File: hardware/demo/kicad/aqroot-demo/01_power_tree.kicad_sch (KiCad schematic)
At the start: 138 parts, among them J3 USB_C_Receptacle_USB2.0_16P, J4 BATTERY PIGTAIL 26AWG, Q2 NTMD4820N, Q3 NTMD4820N, Q4 BSS138, Q5 AO3401A, Q6 BSS138, Q7 BSS138, Q8 BSS138, Q9 BSS138, SW9 SW_SPDT, U10 USBLC6-2SC6, U11 BQ25185, U12 TPS63020, U13 TPS61023, U14 MAX17048, U18 LTC4368-1, U19 TLV7032, U20 TPS22950-Q1, U21 TPS61023, U22 TPS22950-Q1

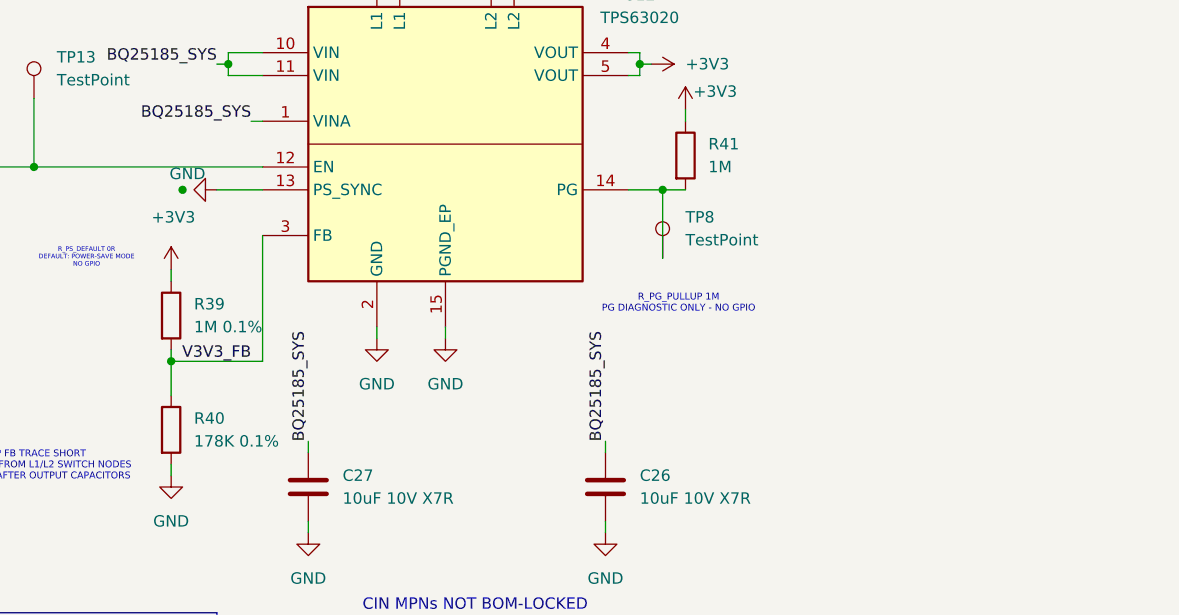
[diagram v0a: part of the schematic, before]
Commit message: demo: D-788 close Round-7 and centre the +3V3 rail inside the display's absolute maximum
Round-7 external review REJECTED D-787.  Astra reproduced 20 observed release
defects (6 high, 6 medium, 8 low) and Fable reproduced a subset plus a sourcing
concern.  All twenty are closed.  Auditing the candidate against its own primary
sources found SIX MORE, R7-N01..R7-N06, and the first two moved the board.

THE HIGH ONE.  The fitted ER-TFT035IPS-6 is an ILI9488 panel whose own datasheet
(archived vendor/ILITEK/ilitek-ili9488-v100.pdf, Table 41) makes 3.3 V the
ABSOLUTE MAXIMUM on both VCI and IOVCC.  D-787's power-save corner stood 242 mV
over it and its NOMINAL stood 9 mV over it.  Closed with two objects and no new
component: U12's PS/SYNC moves GND -> EN (forced fixed-frequency PWM, so TI's
VFB_PS +5 % excursion cannot occur) and the feedback divider moves down.

R7-N01/R7-N02, FOUND HERE.  A DC bound is not the whole high side -- ripple and
load-transient overshoot ride on top of it -- and the low side had NO MCU clause
at all: the rail minimum was checked against the panel's VCI 2.5 V and the
Community Port's published minimum, never against the ESP32-S3-WROOM-1's own
3.0 V VDD33 row.  The first D-788 draft's 187 kOhm left 47.97 mV under a DAMAGE
limit against 86.36 mV over a RECOVERABLE one, which is the wrong way round.
F6 now computes the ripple (1.68 mV pp from SLVS916I's minimum oscillator
frequency and L1's minimum inductance), charges it to both ends, adds the module
floor and the +3V3 plane's bounded distribution drop, and ENUMERATES every
purchasable E192 0.1 % R40 value -- requiring the fitted one to maximise the
smaller of the two headrooms.  R40 is therefore 189 kOhm (YAGEO
RT0603BRD07189KL, C861174, live stock 339), splitting it 76.99 / 58.78 mV.
Load-transient overshoot is deliberately given NO analytic bound, because TI
publishes it only as 50 mV/div plots; it is measured at first article as the new
C-PWR-TRANSIENT-01, and the lever if it fails is C29-C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
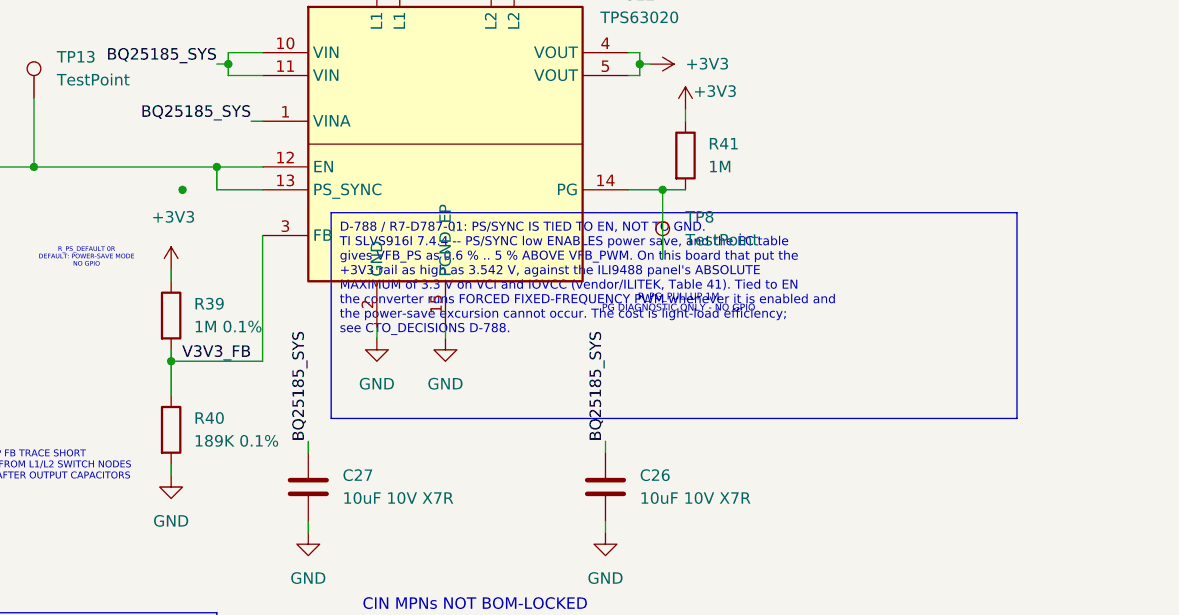
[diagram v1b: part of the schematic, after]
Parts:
- R40: value 178K 0.1% -> 189K 0.1%; LCSC C2441185 -> C861174; MPN ARG03BTC1783 -> RT0603BRD07189KL; Manufacturer Viking Tech -> YAGEO; Note D-787 / R6-A01 THE MAIN 3.3 V RAIL IS ADJUSTABLE AND ITS SE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 -> D-788 / R7-D787-01 + R7-N01. THE RAIL HAD NO CEILING AND TH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; Note_Sourcing SOURCING D-787 2026-09-20, verified live per D-096 through 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 -> SOURCING D-788 2026-09-20, verified live per D-096 through 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
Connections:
- net GND: no longer U12.13 (PS_SYNC)
- net at R43.1, R68.2, SW9.1 (A)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: now also U12.13 (PS_SYNC)
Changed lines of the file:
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@@
 			)
 		)
-		(property "Value" "178K 0.1%"
+		(property "Value" "189K 0.1%"
 			(at 220.98 100.3299 0)
 			(show_name no)
@@
 			)
 		)
-		(property "Manufacturer" "Viking Tech"
+		(property "Manufacturer" "YAGEO"
 			(at 218.44 99.06 0)
 			(hide yes)
@@
 			)
 		)
-		(property "MPN" "ARG03BTC1783"
+		(property "MPN" "RT0603BRD07189KL"
 			(at 218.44 99.06 0)
 			(hide yes)
@@
 			)
 		)
-		(property "LCSC" "C2441185"
+		(property "LCSC" "C861174"
 			(at 218.44 99.06 0)
 			(hide yes)
@@
 			)
 		)
-		(property "Note_Sourcing" "SOURCING D-787 2026-09-20, verified live per D-096 through the JLCPCB parts API.  LCSC C2441185, Viking Tech ARG03BTC1783, 178 kOhm +/-0.1 pct, 0603, 100 mW thin film, +/-25 ppm/C, -55..+155 C, componentLibraryType = expand, stock 3973 (evidence/jlc-live/arg03btc1783-*.json).  SAME Viking ARG03B SERIES AND SAME 0.1 pct / 25 ppm GRADE as R39, so the divider's two halves track.  This REPLACES the D-614 line 'EXACT_PRIOR from the beta-dm audit line 180K 1 pct', which sourced UNI-ROYAL 0603WAF1803T5E C22827.  176 kOhm WAS THE FIRST D-787 CANDIDATE AND IS REFUSED ON AVAILABILITY, not on electricals: every 176 kOhm 0603 part at 0.1 pct or better in the JLCPCB catalogue reads stock 0 -- including the KOA RN73H1JTTD1763B10 C4086101 that draft named (evidence/jlc-live/176k-0603-0-1-*.json) -- so it fails this project's own rule_open_sourcing stock floor of 5 boards x 10 liquidity.  178 kOhm is the nearest STOCKED 0.1 pct value that keeps the derived envelope inside BOTH the 3.135 V Community Port minimum and the 3.600 V internal consumer maximum, and it is also the low-side magnitude TI's own SLVS916I Table 3 prints for a 3.3 V output.  Same 0603 land: no footprint, no copper and no assembly step change."
+		(property "Note_Sourcing" "SOURCING D-788 2026-09-20, verified live per D-096 through the JLCPCB parts API.  LCSC C861174, YAGEO RT0603BRD07189KL, 189 kOhm +/-0.1 pct, 0603, thin film, +/-25 ppm/C, -55..+155 C, componentLibraryType = expand, stock 339 (evidence/jlc-live/rt0603brd07189kl-*.json and 189k-0-1-0603-*.json).  339 is 68x the five-board need of 5 and clears this repository's hard liquidity gate (5 parts x 5 boards x 10 = 50); it is BELOW the 500-piece comfort floor, so rule_open_sourcing carries it as a THIN line and the pre-PCBA stock re-check owns it.  SAME 0.1 pct / 25 ppm GRADE, same YAGEO RT0603 family and the same 0603 land as the 187 kOhm RT0603BRD07187KL C861172 it replaces, so the divider's two halves still track and F6's MPN-keyed temperature-coefficient table needs only the new row.  WAS 187 kOhm RT0603BRD07187KL C861172 (D-788 first draft); WAS 178 kOhm Viking ARG03BTC1783 C2441185 (D-787).  189 kOhm is the E192 value that CENTRES the rail's own tolerance band inside the 3.000..3.300 V window the ESP32-S3 floor and the ILI9488 absolute maximum leave; 191 kOhm overshoots (42.5 mV to the MCU floor) and 188 kOhm is not an E192 value."
 			(at 218.44 99.06 0)
 			(hide yes)
@@
 			)
 		)
-		(property "Note" "D-787 / R6-A01 THE MAIN 3.3 V RAIL IS ADJUSTABLE AND ITS SETPOINT WAS NEVER A PROOF TERM.  Every accessory clause before D-787 ran on a TYPED 3.3 V constant, so the released 1 MOhm / 180 kOhm 1 pct divider could sit anywhere in a band the contract could not see, and F6 stayed green while the Community Port's PUBLISHED 3.135 V minimum was not guaranteed at the PUBLISHED 400 mA.  F6 now DERIVES the whole envelope: TI SLVS916I VFB_PWM 495 / 500 / 505 mV, the fitted value tolerance, the SELECTED PART's temperature coefficient over -40..+85 C, TI's 0.5 pct maximum line and 0.5 pct maximum load regulation applied together, and the +5 pct power-save high side checked separately.  At R39 = 1 MOhm and R40 = 178 kOhm, both Viking ARG03B 0.1 pct / 25 ppm, the raw PWM band is 3.261337 / 3.308989 / 3.357013 V, the heavy-load minimum is 3.228806 V and the power-save high side is 3.542487 V against the 3.600 V tightest internal consumer maximum.  DELIVERY IS A SEPARATE CLAUSE: the bounded hot U20->TP12 prefix, the manual first-five reinforcement lead at its <=30 mOhm acceptance and U20's 68 mOhm maximum RON cost 82.4 mV at 400 mA, leaving 3.146366 V at either duplicated 3.3 V contact.  THE WINDOW IS NARROW IN BOTH DIRECTIONS -- 180 kOhm falls below the connector minimum and 174 kOhm exceeds the internal consumer maximum -- which is why the divider's tolerance grade and temperature coefficient are locked by F7 and why F6 refuses an MPN whose coefficient this repository has not read.  WAS 180 kOhm 1 pct (D-614).  Pinned by checks/demo_feature_contract.py F6 and F7."
+		(property "Note" "D-788 / R7-D787-01 + R7-N01.  THE RAIL HAD NO CEILING AND THE DISPLAY'S ABSOLUTE MAXIMUM IS 3.3 V.  D-787 judged the rail's high side against a 3.600 V 'tightest internal consumer' that was FALSE.  The fitted ER-TFT035IPS-6 is an ILI9488 panel, and ILI Technology's own datasheet -- archived at vendor/ILITEK/ilitek-ili9488-v100.pdf, sha256 aeb23170f809610458e05ab514a5e3017344938ccdba1c2031acb453941df38b, corroborated against a second independent mirror -- gives in Table 41 an ABSOLUTE MAXIMUM of -0.3 .. +3.3 V for BOTH VCI ~ DGND and IOVCC ~ DGND, and in section 17.2 a DC operating range of VCI 2.5 / 2.8 / 3.3 V and IOVCC 1.65 / 1.8 / 3.3 V with VIH max = IOVCC.  D-787's derived power-save high side was 3.542487 V -- 242 mV over an ABSOLUTE MAXIMUM -- and even its NOMINAL 3.308989 V stood 9 mV above it.  D-788 closes it with TWO changes and NO new component: U12's PS/SYNC moves from GND to the EN net so the converter runs FORCED FIXED-FREQUENCY PWM and TI's VFB_PS +5 pct power-save excursion cannot occur, and this divider moves the whole band down.  R7-N01 THEN CENTRES IT: a DC-only bound is not the whole high side, because ripple and load-transient overshoot ride on top of it and TI plots this converter's own load transient at 50 mV/div for a 1 A step (SLVS916I Figures 21/22).  187 kOhm left only 47.97 mV of DC headroom under a DAMAGE limit while leaving 96.99 mV over the ESP32-S3's RECOVERABLE 3.0 V floor; 189 kOhm splits that 76.98 / 69.41 mV, which is where the window centres once the +3V3 plane's own few millivolts of distribution drop are counted on the MCU side.  Raw PWM band 3.100334 / 3.145503 / 3.191022 V, heavy-load minimum 3.069405 V, worst case 3.223016 V.  Display VCI/IOVCC and the MCU remain the SAME net, so VIH <= IOVCC holds by construction and no display input is ever driven above its own supply.  THE COST IS THE COMMUNITY PORT: a rail whose maximum must stay under 3.3 V cannot also guarantee 3.3 V -5 pct at the connector at ANY current.  The owner approved OPTION A on 2026-09-20 and delegated the exact values to the final candidate; this one delivers 2.954958 V at the published 400 mA.  Pinned by checks/demo_feature_contract.py F6 and F7."
 			(at 218.44 99.06 0)
 			(hide yes)
@@
 	(symbol
 		(lib_id "power:GND")
-		(at 223.52 72.39 270)
-		(unit 1)
-		(body_style 1)
-		(exclude_from_sim no)
-		(in_bom yes)
-		(on_board yes)
-		(in_pos_files yes)
-		(dnp no)
-		(property "Reference" "#PWR0146"
-			(at 217.17 72.39 0)
-			(hide yes)
-			(show_name no)
-			(do_not_autoplace no)
-			(effects
-				(font
-					(size 1.27 1.27)
-				)
-			)
-		)
-		(property "Value" "GND"
-			(at 222.25 70.612 90)
-			(show_name no)
-			(do_not_autoplace no)
-			(effects
-				(font
-					(size 1.27 1.27)
-				)
-				(justify right)
-			)
-		)
-		(property "Footprint" ""
-			(at 223.52 72.39 0)
-			(hide yes)
-			(show_name no)
-			(do_not_autoplace no)
-			(effects
-				(font
-					(size 1.27 1.27)
-				)
-			)
-		)
-		(property "Datasheet" ""
-			(at 223.52 72.39 0)
-			(hide yes)
-			(show_name no)
-			(do_not_autoplace no)
-			(effects
-				(font
-					(size 1.27 1.27)
-				)
-			)
-		)
-		(property "Description" "Power symbol creates a global label with name \"GND\" , ground"
-			(at 223.52 72.39 0)
-			(hide yes)
-			(show_name no)
-			(do_not_autoplace no)
-			(effects
-				(font
-					(size 1.27 1.27)
-				)
-			)
-		)
-		(pin "1"
-		)
-		(instances
-			(project "aqroot-Beta-v2"
-				(path "/8a0ad1ee-a49e-4cff-9a78-44823e373405/83b1880a-0a3b-496a-bce6-0dc4c72d8ece"
-					(reference "#PWR0146")
-					(unit 1)
-				)
-			)
-		)
-	)
-	(symbol
-		(lib_id "power:GND")
 		(at 29.21 171.45 0)
 		(unit 1)
@@
 		)
 	)
+	(wire
+		(pts
+			(xy 223.52 72.39) (xy 223.52 69.85)
+		)
+		(stroke
+			(width 0)
+			(type default)
+		)
+	)
+	(junction
+		(at 223.52 69.85)
+		(diameter 0)
+		(color 0 0 0 0)
+	)
+	(text_box "D-788 / R7-D787-01: PS/SYNC IS TIED TO EN, NOT TO GND.\nTI SLVS916I 7.4.4 -- PS/SYNC low ENABLES power save, and the EC table\n gives VFB_PS as 0.6 % .. 5 % ABOVE VFB_PWM. On this board that put the\n+3V3 rail as high as 3.542 V, against the ILI9488 panel's ABSOLUTE\nMAXIMUM of 3.3 V on VCI and IOVCC (vendor/ILITEK, Table 41). Tied to EN\nthe converter runs FORCED FIXED-FREQUENCY PWM whenever it is enabled and\nthe power-save excursion cannot occur. The cost is light-load efficiency;\nsee CTO_DECISIONS D-788."
+		(exclude_from_sim no)
+		(at 236.22 74.93 0)
+		(size 76.2 22.86)
+		(margins 0.9525 0.9525 0.9525 0.9525)
+		(stroke
+			(width 0)
+			(type solid)
+		)
+		(fill
+			(type none)
+		)
+		(effects
+			(font
+				(size 1.0 1.0)
+			)
+			(justify left top)
+		)
+	)
